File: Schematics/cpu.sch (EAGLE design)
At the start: 19 parts, among them IC2 LM555N, IC3 LM555N, U1 74HC245N,652, U2 74HC245N,652, U3 74HC245N,652, U4 74HC04N,652

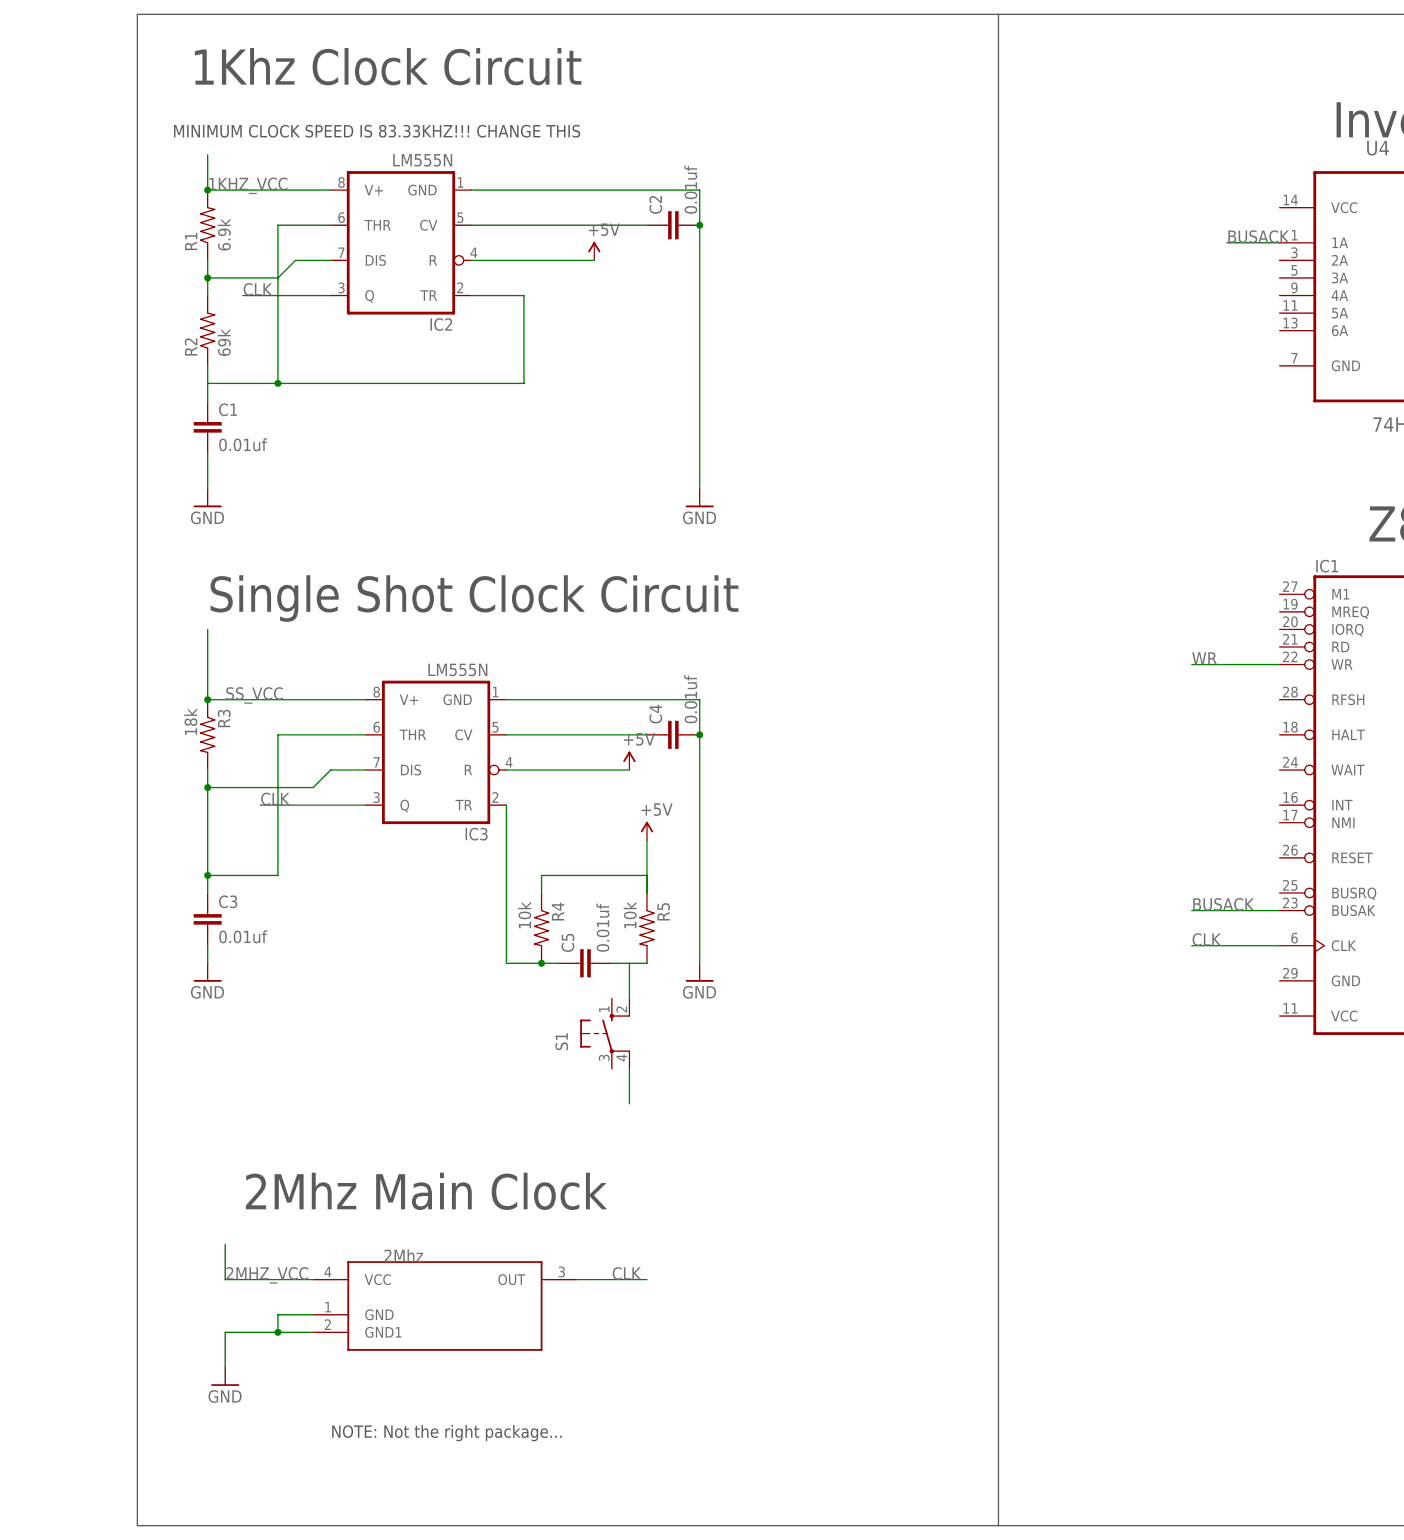
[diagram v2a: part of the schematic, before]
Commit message: added clock select, pwr and gnd to inverter
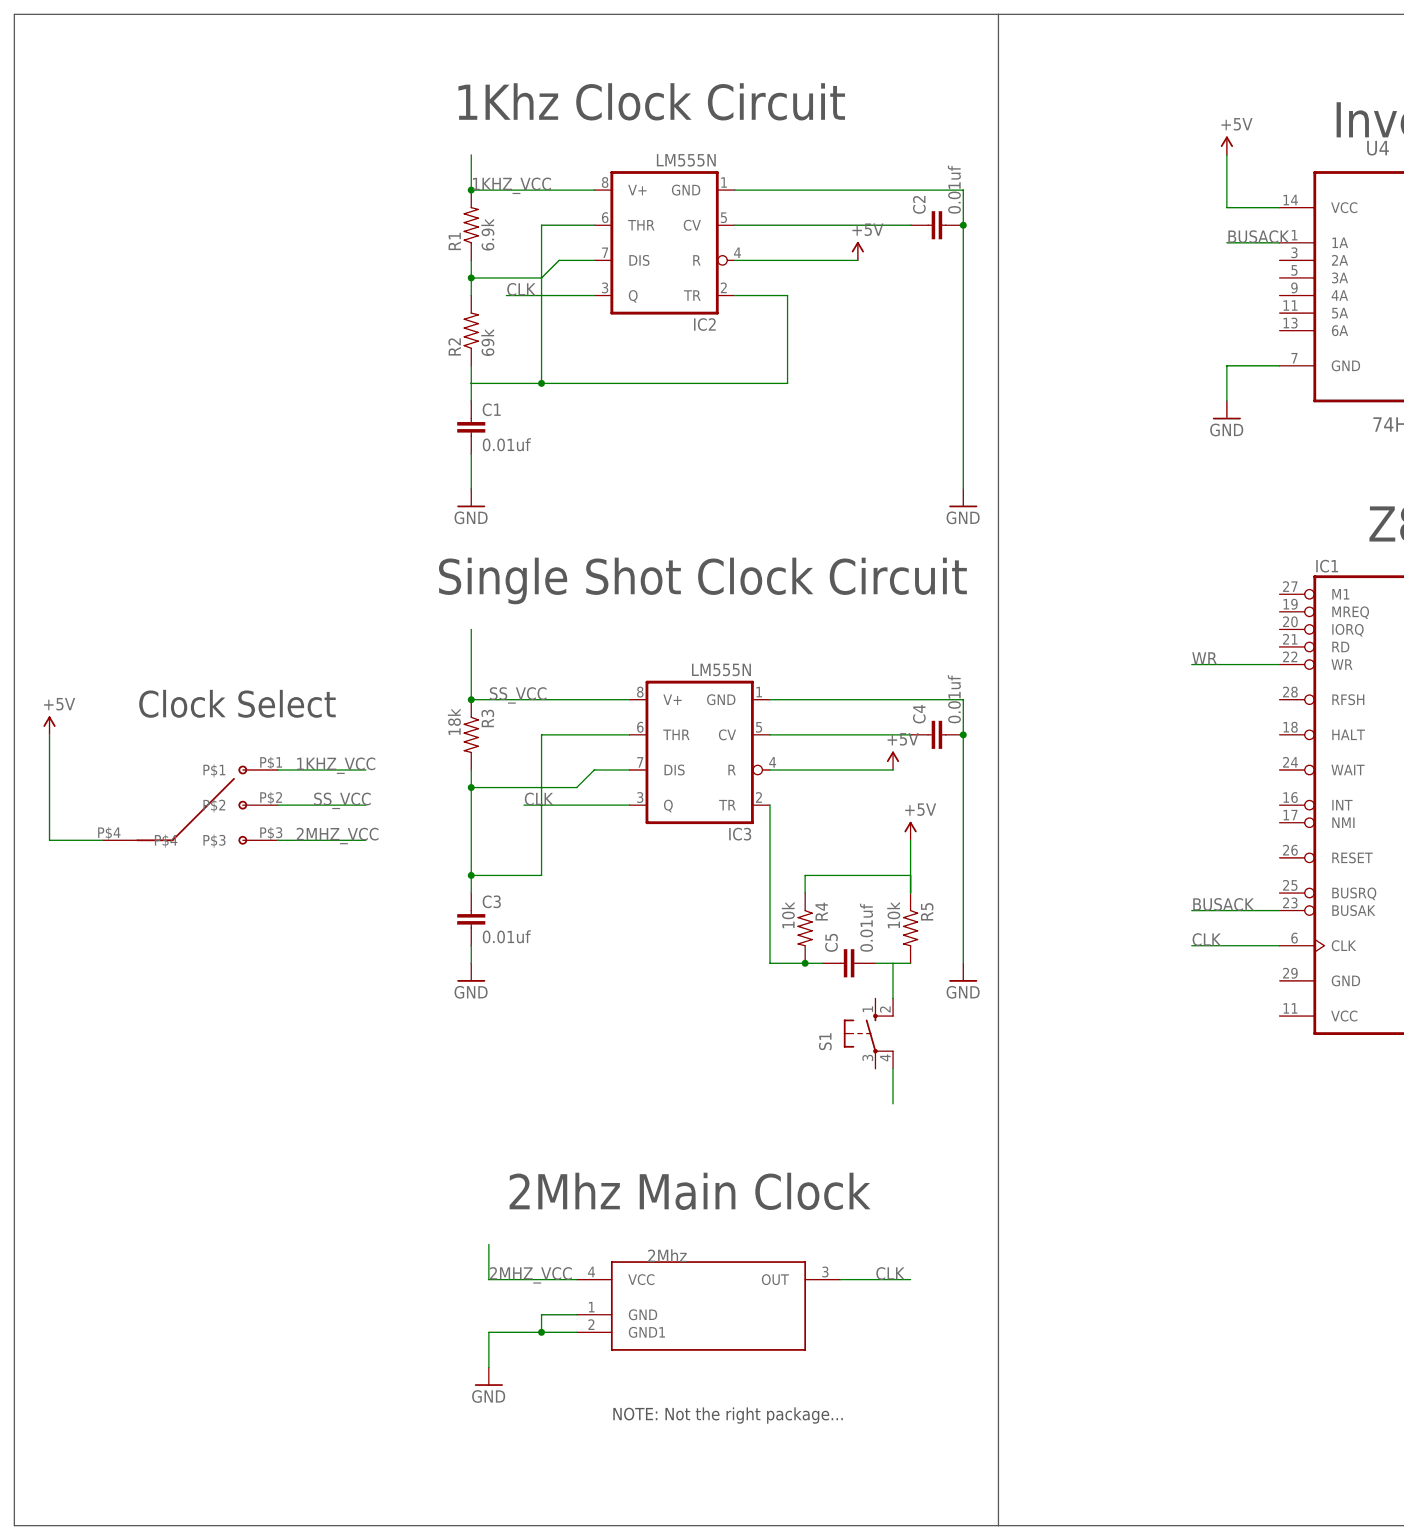
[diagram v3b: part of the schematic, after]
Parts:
- added U$2: 3SWITCH, JakeBooth:3SWITCH
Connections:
- net 1KHZ_VCC: now also U$2.P$1
- net 2MHZ_VCC: now also U$2.P$3
- net GND: now also U4.GND
- net SS_VCC: now also U$2.P$2
- net VCC: now also U$2.P$4, U4.VCC
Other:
- note added: "Clock Select"
- note removed: "MINIMUM CLOCK SPEED IS 83.33KHZ!!! CHANGE THIS"
- moved on the sheet: C1, C2, C3, C4, C5, IC2, IC3, R1, R2, R3, R4, R5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

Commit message: added memory
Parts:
- added U$3: AT28C256-28DIP, atmel-custom:AT28C256-28DIP
- added U$4: HM62256B, JakeBooth:HM62256B
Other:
- note added: "EEPROM"
- note added: "Memory"
- note added: "RAM"
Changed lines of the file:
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@@
 <part name="GND11" library="SparkFun-Aesthetics" deviceset="GND" device=""/>
 <part name="+5V7" library="SparkFun-Aesthetics" deviceset="VCC" device="" value="+5V"/>
+<part name="U$3" library="atmel-custom" deviceset="AT28C256-28DIP" device=""/>
+<part name="U$4" library="JakeBooth" deviceset="HM62256B" device=""/>
 </parts>
 <sheets>
@@
 <text x="-104.14" y="-33.02" size="5.08" layer="97">2Mhz Main Clock</text>
 <text x="-157.48" y="38.1" size="3.81" layer="97">Clock Select</text>
+<text x="-162.56" y="12.7" size="1.778" layer="97">NOTE: Not the right package...</text>
+<wire x1="182.88" y1="139.7" x2="340.36" y2="139.7" width="0.1524" layer="97"/>
+<wire x1="340.36" y1="139.7" x2="340.36" y2="-78.74" width="0.1524" layer="97"/>
+<wire x1="340.36" y1="-78.74" x2="182.88" y2="-78.74" width="0.1524" layer="97"/>
+<text x="276.86" y="96.52" size="3.81" layer="97">EEPROM</text>
+<text x="284.48" y="0" size="3.81" layer="97">RAM</text>
+<text x="246.38" y="124.46" size="6.4516" layer="97">Memory </text>
 </plain>
 <instances>
@@
 <instance part="GND11" gate="1" x="0" y="81.28"/>
 <instance part="+5V7" gate="G$1" x="0" y="119.38"/>
+<instance part="U$3" gate="G$1" x="281.94" y="88.9"/>
+<instance part="U$4" gate="G$1" x="292.1" y="-25.4"/>
 </instances>
 <busses>

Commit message: added or gate, too late to think streight
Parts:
- added U5: 74HC32N,652, NXP_By_element14_Batch_1:74HC32N,652
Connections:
- new net IORQ: IC1.IORQ
- new net MREQ: IC1.MREQ
- new net N$32: U5.1A
- new net N$34: U5.1B
- new net RD: IC1.RD
- net GND: now also U$3.A14, U$3.GND, U$4.A14, U$4.VSS, U5.GND
- net VCC: now also U5.VCC
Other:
- note added: "32kb EEPROM"
- note added: "32kb RAM"
- note removed: "EEPROM"
- note removed: "RAM"
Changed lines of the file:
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@@
 <?xml version="1.0" encoding="utf-8"?>
 <!DOCTYPE eagle SYSTEM "eagle.dtd">
-<eagle version="6.5.0">
+<eagle version="7.5.0">
 <drawing>
 <settings>
@@
 <part name="U$3" library="atmel-custom" deviceset="AT28C256-28DIP" device=""/>
 <part name="U$4" library="JakeBooth" deviceset="HM62256B" device=""/>
+<part name="GND12" library="SparkFun-Aesthetics" deviceset="GND" device=""/>
+<part name="GND13" library="SparkFun-Aesthetics" deviceset="GND" device=""/>
+<part name="GND14" library="SparkFun-Aesthetics" deviceset="GND" device=""/>
+<part name="U5" library="NXP_By_element14_Batch_1" deviceset="74HC32N,652" device=""/>
+<part name="+5V8" library="SparkFun-Aesthetics" deviceset="VCC" device="" value="+5V"/>
+<part name="GND15" library="SparkFun-Aesthetics" deviceset="GND" device=""/>
 </parts>
 <sheets>
@@
 <wire x1="340.36" y1="139.7" x2="340.36" y2="-78.74" width="0.1524" layer="97"/>
 <wire x1="340.36" y1="-78.74" x2="182.88" y2="-78.74" width="0.1524" layer="97"/>
-<text x="276.86" y="96.52" size="3.81" layer="97">EEPROM</text>
-<text x="284.48" y="0" size="3.81" layer="97">RAM</text>
+<text x="276.86" y="96.52" size="3.81" layer="97">32kb EEPROM</text>
+<text x="281.94" y="0" size="3.81" layer="97">32kb RAM</text>
 <text x="246.38" y="124.46" size="6.4516" layer="97">Memory </text>
 </plain>
@@
 <instance part="U$3" gate="G$1" x="281.94" y="88.9"/>
 <instance part="U$4" gate="G$1" x="292.1" y="-25.4"/>
+<instance part="GND12" gate="1" x="264.16" y="33.02"/>
+<instance part="GND13" gate="1" x="269.24" y="-50.8"/>
+<instance part="GND14" gate="1" x="322.58" y="-50.8"/>
+<instance part="U5" gate="A" x="226.06" y="71.12"/>
+<instance part="+5V8" gate="G$1" x="200.66" y="91.44"/>
+<instance part="GND15" gate="1" x="200.66" y="43.18"/>
 </instances>
 <busses>
@@
 <pinref part="GND11" gate="1" pin="GND"/>
 </segment>
+<segment>
+<pinref part="U$3" gate="G$1" pin="A14"/>
+<wire x1="276.86" y1="50.8" x2="264.16" y2="50.8" width="0.1524" layer="91"/>
+<wire x1="264.16" y1="50.8" x2="264.16" y2="40.64" width="0.1524" layer="91"/>
+<pinref part="U$3" gate="G$1" pin="GND"/>
+<wire x1="276.86" y1="40.64" x2="264.16" y2="40.64" width="0.1524" layer="91"/>
+<wire x1="264.16" y1="40.64" x2="264.16" y2="35.56" width="0.1524" layer="91"/>
+<pinref part="GND12" gate="1" pin="GND"/>
+</segment>
+<segment>
+<pinref part="U$4" gate="G$1" pin="A14"/>
+<wire x1="276.86" y1="-40.64" x2="269.24" y2="-40.64" width="0.1524" layer="91"/>
+<wire x1="269.24" y1="-40.64" x2="269.24" y2="-48.26" width="0.1524" layer="91"/>
+<pinref part="GND13" gate="1" pin="GND"/>
+</segment>
+<segment>
+<pinref part="U$4" gate="G$1" pin="VSS"/>
+<wire x1="307.34" y1="-33.02" x2="322.58" y2="-33.02" width="0.1524" layer="91"/>
+<wire x1="322.58" y1="-33.02" x2="322.58" y2="-48.26" width="0.1524" layer="91"/>
+<pinref part="GND14" gate="1" pin="GND"/>
+</segment>
+<segment>
+<pinref part="U5" gate="A" pin="GND"/>
+<wire x1="208.28" y1="53.34" x2="200.66" y2="53.34" width="0.1524" layer="91"/>
+<wire x1="200.66" y1="53.34" x2="200.66" y2="45.72" width="0.1524" layer="91"/>
+<pinref part="GND15" gate="1" pin="GND"/>
+</segment>
 </net>
 <net name="N$18" class="0">
@@
 <wire x1="0" y1="111.76" x2="0" y2="119.38" width="0.1524" layer="91"/>
 <pinref part="+5V7" gate="G$1" pin="VCC"/>
+</segment>
+<segment>
+<pinref part="U5" gate="A" pin="VCC"/>
+<wire x1="208.28" y1="83.82" x2="200.66" y2="83.82" width="0.1524" layer="91"/>
+<wire x1="200.66" y1="83.82" x2="200.66" y2="91.44" width="0.1524" layer="91"/>
+<pinref part="+5V8" gate="G$1" pin="VCC"/>
 </segment>
 </net>
@@
 </segment>
 </net>
+<net name="MREQ" class="0">
+<segment>
+<pinref part="IC1" gate="1" pin="MREQ"/>
+<wire x1="7.62" y1="53.34" x2="-5.08" y2="53.34" width="0.1524" layer="91"/>
+<label x="-5.08" y="53.34" size="1.778" layer="95"/>
+</segment>
+</net>
+<net name="RD" class="0">
+<segment>
+<pinref part="IC1" gate="1" pin="RD"/>
+<wire x1="7.62" y1="48.26" x2="-5.08" y2="48.26" width="0.1524" layer="91"/>
+<label x="-5.08" y="48.26" size="1.778" layer="95"/>
+</segment>
+</net>
+<net name="IORQ" class="0">
+<segment>
+<pinref part="IC1" gate="1" pin="IORQ"/>
+<wire x1="7.62" y1="50.8" x2="-5.08" y2="50.8" width="0.1524" layer="91"/>
+<label x="-5.08" y="50.8" size="1.778" layer="95"/>
+</segment>
+</net>
+<net name="N$32" class="0">
+<segment>
+<pinref part="U5" gate="A" pin="1A"/>
+<wire x1="200.66" y1="66.04" x2="208.28" y2="66.04" width="0.1524" layer="91"/>
+</segment>
+</net>
+<net name="N$34" class="0">
+<segment>
+<pinref part="U5" gate="A" pin="1B"/>
+<wire x1="200.66" y1="78.74" x2="208.28" y2="78.74" width="0.1524" layer="91"/>
+</segment>
+</net>

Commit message: Added data and adderess busses, added bus debug header
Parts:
- added JP1: (no value), pinhead:PINHD-1X16
- added JP2: (no value), pinhead:PINHD-1X8
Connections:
- net ADD0: now also JP1.1, U$3.A0, U$4.A0
- net ADD1: now also JP1.2, U$3.A1, U$4.A1
- net ADD10: now also JP1.11, U$3.A10, U$4.A10
- net ADD11: now also JP1.12, U$3.A11, U$4.A11
- net ADD12: now also JP1.13, U$3.A12, U$4.A12
- net ADD13: now also JP1.14
- net ADD14: now also JP1.15
- net ADD15: now also JP1.16
- net ADD2: now also JP1.3, U$3.A2, U$4.A2
- net ADD3: now also JP1.4, U$3.A3, U$4.A3
- net ADD4: now also JP1.5, U$3.A4, U$4.A4
- net ADD5: now also JP1.6, U$3.A5, U$4.A5
- net ADD6: now also JP1.7, U$3.A6, U$4.A6
- net ADD7: now also JP1.8, U$3.A7, U$4.A7
- net ADD8: now also JP1.9, U$3.A8, U$4.A8
- net ADD9: now also JP1.10, U$3.A9, U$4.A9
- net DAT0: now also JP2.1, U$3.I/O0, U$4.I/O0
- net DAT1: now also JP2.2, U$3.I/O1, U$4.I/O1
- net DAT2: now also JP2.3, U$3.I/O2, U$4.I/O2
- net DAT3: now also JP2.4, U$3.I/O3, U$4.I/O3
- net DAT4: now also JP2.5, U$3.I/O4, U$4.I/O4
- net DAT5: now also JP2.6, U$3.I/O5, U$4.I/O5
- net DAT6: now also JP2.7, U$3.I/O6, U$4.I/O6
- net DAT7: now also JP2.8, U$3.I/O7, U$4.I/O7
- net GND: now also IC1.GND
- net VCC: now also IC1.VCC
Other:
- note added: "Address Debug"
- note added: "Data Debug"
- moved on the sheet: U$3, U5

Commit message: added datasheets. Finished memory decoding logic. 16k rom, 16k ram
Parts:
- removed U5: 74HC32N,652, NXP_By_element14_Batch_1:74HC32N,652
- added IC4: 7400N, 74xx-us:7400N
- added IC5: 74LS32N, 74xx-us:74LS32N
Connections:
- new net N$35: IC5C.O, U$3./OE, U$4.OE
- new net N$36: IC4A.O, U$4.CS
- new net N$37: IC4A.I1, IC4B.O
- net ADD13: now also U$3.A13, U$4.A13
- net ADD14: now also IC4A.I0, IC5B.I0
- net ADD15: now also IC4B.I0, IC4B.I1, IC5B.I1
- net GND: no longer U5.GND
- net MREQ: now also IC5A.I1, IC5C.I1
- net N$32: now also IC5B.O, U$3./CE; no longer U5.1A
- net N$34: now also IC5A.O, U$3./WE, U$4.WE; no longer U5.1B
- net RD: now also IC5C.I0
- net VCC: now also U$3.VCC, U$4.VCC; no longer U5.VCC
- net WR: now also IC5A.I0
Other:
- note added: "First 16k is ROM, second 16k is RAM. Last 32k is currently unused"
- note added: "ROM Addresses: 0x000 - 0x3FFF"
- note added: "Ram Addresses: 0x4000 - 0x7FFF"
- moved on the sheet: JP1, JP2, U$3

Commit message: added input latches, input arduino
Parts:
- added I/O1, I/O10, I/O11, I/O12, I/O13, I/O14, I/O15, I/O16, I/O2, I/O3, I/O4, I/O5, I/O6, I/O7, I/O8, I/O9: 74AS573N, 74xx-us:74AS573N
- added IC22: 74154N, 74xx-us:74154N
- added IC6: ATMEGA328-20P, atmega328:ATMEGA328-20P
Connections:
- new net BUSRQ: IC1.BUSRQ
- new net I/ODAT0: I/O10A.1D, I/O11A.1D, I/O12A.1D, I/O13A.1D, I/O14A.1D, I/O15A.1D, I/O16A.1D, I/O1A.1D, I/O3A.1D, I/O4A.1D, I/O5A.1D, I/O6A.1D, I/O7A.1D, I/O8A.1D, I/O9A.1D
- new net I/ODAT1: I/O10A.2D, I/O11A.2D, I/O12A.2D, I/O13A.2D, I/O14A.2D, I/O15A.2D, I/O16A.2D, I/O1A.2D, I/O3A.2D, I/O4A.2D, I/O5A.2D, I/O6A.2D, I/O7A.2D, I/O8A.2D, I/O9A.2D
- new net I/ODAT2: I/O10A.3D, I/O11A.3D, I/O12A.3D, I/O13A.3D, I/O14A.3D, I/O15A.3D, I/O16A.3D, I/O1A.3D, I/O3A.3D, I/O4A.3D, I/O5A.3D, I/O6A.3D, I/O7A.3D, I/O8A.3D, I/O9A.3D
- new net I/ODAT3: I/O10A.4D, I/O11A.4D, I/O12A.4D, I/O13A.4D, I/O14A.4D, I/O15A.4D, I/O16A.4D, I/O1A.4D, I/O3A.4D, I/O4A.4D, I/O5A.4D, I/O6A.4D, I/O7A.4D, I/O8A.4D, I/O9A.4D
- new net I/ODAT4: I/O10A.5D, I/O11A.5D, I/O12A.5D, I/O13A.5D, I/O14A.5D, I/O15A.5D, I/O16A.5D, I/O1A.5D, I/O3A.5D, I/O4A.5D, I/O5A.5D, I/O6A.5D, I/O7A.5D, I/O8A.5D, I/O9A.5D
- new net I/ODAT5: I/O10A.6D, I/O11A.6D, I/O12A.6D, I/O13A.6D, I/O14A.6D, I/O15A.6D, I/O16A.6D, I/O1A.6D, I/O3A.6D, I/O4A.6D, I/O5A.6D, I/O6A.6D, I/O7A.6D, I/O8A.6D, I/O9A.6D
- new net I/ODAT6: I/O10A.7D, I/O11A.7D, I/O12A.7D, I/O13A.7D, I/O14A.7D, I/O15A.7D, I/O16A.7D, I/O1A.7D, I/O3A.7D, I/O4A.7D, I/O5A.7D, I/O6A.7D, I/O7A.7D, I/O8A.7D, I/O9A.7D
- new net I/ODAT7: I/O10A.8D, I/O11A.8D, I/O12A.8D, I/O13A.8D, I/O14A.8D, I/O15A.8D, I/O16A.8D, I/O1A.8D, I/O3A.8D, I/O4A.8D, I/O5A.8D, I/O6A.8D, I/O7A.8D, I/O8A.8D, I/O9A.8D
- new net INT: IC1.INT
- new net IORD: IC22A.G1, IC22A.G2, IC5D.O
- new net N$38: I/O1A.OC, IC22A.0
- new net N$39: I/O2A.OC, IC22A.1
- new net N$40: I/O3A.OC, IC22A.2
- new net N$41: I/O4A.OC, IC22A.3
- new net N$42: I/O5A.OC, IC22A.4
- new net N$43: I/O6A.OC, IC22A.5
- new net N$44: I/O7A.OC, IC22A.6
- new net N$45: I/O8A.OC, IC22A.7
- new net N$46: I/O9A.OC, IC22A.8
- new net N$47: I/O10A.OC, IC22A.9
- new net N$48: I/O11A.OC, IC22A.10
- new net N$49: I/O12A.OC, IC22A.11
- new net N$50: I/O13A.OC, IC22A.12
- new net N$51: I/O15A.OC, IC22A.13
- new net N$52: I/O16A.OC, IC22A.14
- new net N$53: IC6.(PCI18/INT0)PD2
- new net N$54: IC6.(PCI19/INT1/OC2B)PD3
- new net N$55: IC6.(PCI12/ADC4/SDA)PC4
- new net N$56: IC6.(PCI13/ADC5/SCL)PC5
- new net N$57: IC6.(PCI16/RXD)PD0
- new net N$58: IC6.(PCI17/TXD)PD1
- new net N$59: IC6.(PCI5/SCK)PB5
- new net N$60: IC6.(PCI4/MISO)PB4
- new net N$61: IC6.(PCI3/MOSI/OC2A)PB3
- new net N$62: IC6.(PCI2/SS/OC1B)PB2
- new net N$63: IC6.(PCI21/T1/OC0B)PD5
- new net NMI: IC1.NMI
- net ADD0: now also IC22A.A
- net ADD1: now also IC22A.B
- net ADD2: now also IC22A.C
- net ADD3: now also IC22A.D
- net DAT0: now also I/O10A.1Q, I/O11A.1Q, I/O12A.1Q, I/O13A.1Q, I/O14A.1Q, I/O15A.1Q, I/O16A.1Q, I/O1A.1Q, I/O2A.1Q, I/O3A.1Q, I/O4A.1Q, I/O5A.1Q, I/O6A.1Q, I/O7A.1Q, I/O8A.1Q, I/O9A.1Q
- net DAT1: now also I/O10A.2Q, I/O11A.2Q, I/O12A.2Q, I/O13A.2Q, I/O14A.2Q, I/O15A.2Q, I/O16A.2Q, I/O1A.2Q, I/O2A.2Q, I/O3A.2Q, I/O4A.2Q, I/O5A.2Q, I/O6A.2Q, I/O7A.2Q, I/O8A.2Q, I/O9A.2Q
- net DAT2: now also I/O10A.3Q, I/O11A.3Q, I/O12A.3Q, I/O13A.3Q, I/O14A.3Q, I/O15A.3Q, I/O16A.3Q, I/O1A.3Q, I/O2A.3Q, I/O3A.3Q, I/O4A.3Q, I/O5A.3Q, I/O6A.3Q, I/O7A.3Q, I/O8A.3Q, I/O9A.3Q
- net DAT3: now also I/O10A.4Q, I/O11A.4Q, I/O12A.4Q, I/O13A.4Q, I/O14A.4Q, I/O15A.4Q, I/O16A.4Q, I/O1A.4Q, I/O2A.4Q, I/O3A.4Q, I/O4A.4Q, I/O5A.4Q, I/O6A.4Q, I/O7A.4Q, I/O8A.4Q, I/O9A.4Q
- net DAT4: now also I/O10A.5Q, I/O11A.5Q, I/O12A.5Q, I/O13A.5Q, I/O14A.5Q, I/O15A.5Q, I/O16A.5Q, I/O1A.5Q, I/O2A.5Q, I/O3A.5Q, I/O4A.5Q, I/O5A.5Q, I/O6A.5Q, I/O7A.5Q, I/O8A.5Q, I/O9A.5Q
- net DAT5: now also I/O10A.6Q, I/O11A.6Q, I/O12A.6Q, I/O13A.6Q, I/O14A.6Q, I/O15A.6Q, I/O16A.6Q, I/O1A.6Q, I/O2A.6Q, I/O3A.6Q, I/O4A.6Q, I/O5A.6Q, I/O6A.6Q, I/O7A.6Q, I/O8A.6Q, I/O9A.6Q
- net DAT6: now also I/O10A.7Q, I/O11A.7Q, I/O12A.7Q, I/O13A.7Q, I/O14A.7Q, I/O15A.7Q, I/O16A.7Q, I/O1A.7Q, I/O2A.7Q, I/O3A.7Q, I/O4A.7Q, I/O5A.7Q, I/O6A.7Q, I/O7A.7Q, I/O8A.7Q, I/O9A.7Q
- net DAT7: now also I/O10A.8Q, I/O11A.8Q, I/O12A.8Q, I/O13A.8Q, I/O14A.8Q, I/O15A.8Q, I/O16A.8Q, I/O1A.8Q, I/O2A.8Q, I/O3A.8Q, I/O4A.8Q, I/O5A.8Q, I/O6A.8Q, I/O7A.8Q, I/O8A.8Q, I/O9A.8Q
- net IORQ: now also IC5D.I1
- net RD: now also IC5D.I0
